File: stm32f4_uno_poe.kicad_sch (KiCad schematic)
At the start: 12 parts, among them J101 STM32 GPIO, J102 Digital/PWM, J103 STM32 GPIO, J104 STM32 GPIO, J105 STM32 GPIO, J106 Power, J107 Conn_01x04, J108 Ethernet, J109 STM32 GPIO, J110 Digital/PWM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

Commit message: WIP
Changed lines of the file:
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@@
     )
     (property "Description" "" (at 262.255 37.465 0)
-      (effects (font (size 1.27 1.27)) hide)
+      (effects (font (size 1 1)) hide)
     )
     (property "Manufacturer" "" (at 262.255 37.465 0)
-      (effects (font (size 1.27 1.27)) hide)
+      (effects (font (size 1 1)) hide)
     )
     (property "Partnumber" "" (at 262.255 37.465 0)
-      (effects (font (size 1.27 1.27)) hide)
+      (effects (font (size 1 1)) hide)
     )
     (property "JLCPCB Part #" "" (at 262.255 37.465 0)
-      (effects (font (size 1.27 1.27)) hide)
+      (effects (font (size 1 1)) hide)
     )
     (property "isBasicPart" "" (at 262.255 37.465 0)
-      (effects (font (size 1.27 1.27)) hide)
+      (effects (font (size 1 1)) hide)
     )
     (property "Description" "" (at 262.255 37.465 0)
-      (effects (font (size 1.27 1.27)) hide)
+      (effects (font (size 1 1)) hide)
     )
     (property "Manufacturer" "" (at 262.255 37.465 0)
-      (effects (font (size 1.27 1.27)) hide)
+      (effects (font (size 1 1)) hide)
     )
     (property "Partnumber" "" (at 262.255 37.465 0)
-      (effects (font (size 1.27 1.27)) hide)
+      (effects (font (size 1 1)) hide)
     )
     (property "JLCPCB Part #" "" (at 262.255 37.465 0)
-      (effects (font (size 1.27 1.27)) hide)
+      (effects (font (size 1 1)) hide)
     )
     (property "isBasicPart" "" (at 262.255 37.465 0)
-      (effects (font (size 1.27 1.27)) hide)
+      (effects (font (size 1 1)) hide)
     )
     (pin "1")
@@
     )
     (property "Description" "" (at 262.255 67.945 0)
-      (effects (font (size 1.27 1.27)) hide)
+      (effects (font (size 1 1)) hide)
     )
     (property "Manufacturer" "" (at 262.255 67.945 0)
-      (effects (font (size 1.27 1.27)) hide)
+      (effects (font (size 1 1)) hide)
     )
     (property "Partnumber" "" (at 262.255 67.945 0)
-      (effects (font (size 1.27 1.27)) hide)
+      (effects (font (size 1 1)) hide)
     )
     (property "JLCPCB Part #" "" (at 262.255 67.945 0)
-      (effects (font (size 1.27 1.27)) hide)
+      (effects (font (size 1 1)) hide)
     )
     (property "isBasicPart" "" (at 262.255 67.945 0)
-      (effects (font (size 1.27 1.27)) hide)
+      (effects (font (size 1 1)) hide)
     )
     (property "Description" "" (at 262.255 67.945 0)
-      (effects (font (size 1.27 1.27)) hide)
+      (effects (font (size 1 1)) hide)
     )
     (property "Manufacturer" "" (at 262.255 67.945 0)
-      (effects (font (size 1.27 1.27)) hide)
+      (effects (font (size 1 1)) hide)
     )
     (property "Partnumber" "" (at 262.255 67.945 0)
-      (effects (font (size 1.27 1.27)) hide)
+      (effects (font (size 1 1)) hide)
     )
     (property "JLCPCB Part #" "" (at 262.255 67.945 0)
-      (effects (font (size 1.27 1.27)) hide)
+      (effects (font (size 1 1)) hide)
     )
     (property "isBasicPart" "" (at 262.255 67.945 0)
-      (effects (font (size 1.27 1.27)) hide)
+      (effects (font (size 1 1)) hide)
     )
     (pin "1")
@@
     (in_bom yes) (on_board yes) (dnp yes) (fields_autoplaced)
     (property "Reference" "J112" (at 52.07 69.215 0)
-      (effects (font (size 1.27 1.27)))
+      (effects (font (size 1 1)))
     )
     (property "Value" "Barrel_Jack" (at 52.07 71.755 0)
-      (effects (font (size 1.27 1.27)))
+      (effects (font (size 1 1)))
     )
     (property "Footprint" "Connector_BarrelJack:BarrelJack_CUI_PJ-102AH_Horizontal" (at 53.34 78.486 0)
-      (effects (font (size 1.27 1.27)) hide)
+      (effects (font (size 1 1)) hide)
     )
     (property "Datasheet" "~" (at 53.34 78.486 0)
-      (effects (font (size 1.27 1.27)) hide)
+      (effects (font (size 1 1)) hide)
     )
     (property "Description" "" (at 52.07 77.47 0)
-      (effects (font (size 1.27 1.27)) hide)
+      (effects (font (size 1 1)) hide)
     )
     (property "Manufacturer" "CUI Devices" (at 52.07 77.47 0)
-      (effects (font (size 1.27 1.27)) hide)
+      (effects (font (size 1 1)) hide)
     )
     (property "Partnumber" "PJ-102AH" (at 52.07 77.47 0)
-      (effects (font (size 1.27 1.27)) hide)
+      (effects (font (size 1 1)) hide)
     )
     (property "JLCPCB Part #" "" (at 52.07 77.47 0)
-      (effects (font (size 1.27 1.27)) hide)
+      (effects (font (size 1 1)) hide)
     )
     (property "isBasicPart" "NO" (at 52.07 77.47 0)
-      (effects (font (size 1.27 1.27)) hide)
+      (effects (font (size 1 1)) hide)
     )
     (pin "1")
@@
     )
     (property "Description" "" (at 54.61 59.69 0)
-      (effects (font (size 1.27 1.27)) hide)
+      (effects (font (size 1 1)) hide)
     )
     (property "Manufacturer" "" (at 54.61 59.69 0)
-      (effects (font (size 1.27 1.27)) hide)
+      (effects (font (size 1 1)) hide)
     )
     (property "Partnumber" "" (at 54.61 59.69 0)
-      (effects (font (size 1.27 1.27)) hide)
+      (effects (font (size 1 1)) hide)
     )
     (property "JLCPCB Part #" "" (at 54.61 59.69 0)
-      (effects (font (size 1.27 1.27)) hide)
+      (effects (font (size 1 1)) hide)
     )
     (property "isBasicPart" "" (at 54.61 59.69 0)
-      (effects (font (size 1.27 1.27)) hide)
+      (effects (font (size 1 1)) hide)
     )
     (property "Description" "" (at 54.61 59.69 0)
-      (effects (font (size 1.27 1.27)) hide)
+      (effects (font (size 1 1)) hide)
     )
     (property "Manufacturer" "" (at 54.61 59.69 0)
-      (effects (font (size 1.27 1.27)) hide)
+      (effects (font (size 1 1)) hide)
     )
     (property "Partnumber" "" (at 54.61 59.69 0)
-      (effects (font (size 1.27 1.27)) hide)
+      (effects (font (size 1 1)) hide)
     )
     (property "JLCPCB Part #" "" (at 54.61 59.69 0)
-      (effects (font (size 1.27 1.27)) hide)
+      (effects (font (size 1 1)) hide)
     )
     (property "isBasicPart" "" (at 54.61 59.69 0)
-      (effects (font (size 1.27 1.27)) hide)
+      (effects (font (size 1 1)) hide)
     )
     (pin "1")
@@
     )
     (property "Description" "" (at 204.47 42.545 0)
-      (effects (font (size 1.27 1.27)) hide)
+      (effects (font (size 1 1)) hide)
     )
     (property "Manufacturer" "" (at 204.47 42.545 0)
-      (effects (font (size 1.27 1.27)) hide)
+      (effects (font (size 1 1)) hide)
     )
     (property "Partnumber" "" (at 204.47 42.545 0)
-      (effects (font (size 1.27 1.27)) hide)
+      (effects (font (size 1 1)) hide)
     )
     (property "JLCPCB Part #" "" (at 204.47 42.545 0)
-      (effects (font (size 1.27 1.27)) hide)
+      (effects (font (size 1 1)) hide)
     )
     (property "isBasicPart" "" (at 204.47 42.545 0)
-      (effects (font (size 1.27 1.27)) hide)
+      (effects (font (size 1 1)) hide)
     )
     (property "Description" "" (at 204.47 42.545 0)
-      (effects (font (size 1.27 1.27)) hide)
+      (effects (font (size 1 1)) hide)
     )
     (property "Manufacturer" "" (at 204.47 42.545 0)
-      (effects (font (size 1.27 1.27)) hide)
+      (effects (font (size 1 1)) hide)
     )
     (property "Partnumber" "" (at 204.47 42.545 0)
-      (effects (font (size 1.27 1.27)) hide)
+      (effects (font (size 1 1)) hide)
     )
     (property "JLCPCB Part #" "" (at 204.47 42.545 0)
-      (effects (font (size 1.27 1.27)) hide)
+      (effects (font (size 1 1)) hide)
     )
     (property "isBasicPart" "" (at 204.47 42.545 0)
-      (effects (font (size 1.27 1.27)) hide)
+      (effects (font (size 1 1)) hide)
     )
     (pin "1")
@@
     )
     (property "Description" "" (at 204.47 67.945 0)
-      (effects (font (size 1.27 1.27)) hide)
+      (effects (font (size 1 1)) hide)
     )
     (property "Manufacturer" "" (at 204.47 67.945 0)
-      (effects (font (size 1.27 1.27)) hide)
+      (effects (font (size 1 1)) hide)
     )
     (property "Partnumber" "" (at 204.47 67.945 0)
-      (effects (font (size 1.27 1.27)) hide)
+      (effects (font (size 1 1)) hide)
     )
     (property "JLCPCB Part #" "" (at 204.47 67.945 0)
-      (effects (font (size 1.27 1.27)) hide)
+      (effects (font (size 1 1)) hide)
     )
     (property "isBasicPart" "" (at 204.47 67.945 0)
-      (effects (font (size 1.27 1.27)) hide)
+      (effects (font (size 1 1)) hide)
     )
     (property "Description" "" (at 204.47 67.945 0)
-      (effects (font (size 1.27 1.27)) hide)
+      (effects (font (size 1 1)) hide)
     )
     (property "Manufacturer" "" (at 204.47 67.945 0)
-      (effects (font (size 1.27 1.27)) hide)
+      (effects (font (size 1 1)) hide)
     )
     (property "Partnumber" "" (at 204.47 67.945 0)
-      (effects (font (size 1.27 1.27)) hide)
+      (effects (font (size 1 1)) hide)
     )
     (property "JLCPCB Part #" "" (at 204.47 67.945 0)
-      (effects (font (size 1.27 1.27)) hide)
+      (effects (font (size 1 1)) hide)
     )
     (property "isBasicPart" "" (at 204.47 67.945 0)
-      (effects (font (size 1.27 1.27)) hide)
-    )
-    (pin "1")
+      (effects (font (size 1 1)) hide)
+    )
+    (pin "1")

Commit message: WIP
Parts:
- added J113: Conn_01x02, symbol Connector_Generic:Conn_01x02
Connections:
- net GND: now also J113.2 (Pin_2)
- net PoE/24V: now also J113.1 (Pin_1)
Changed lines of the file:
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@@
     (stroke (width 0) (type solid))
+  )
+  (wire (pts (xy 119.38 57.15) (xy 123.19 57.15))
+    (stroke (width 0) (type default))
   )
   (wire (pts (xy 172.085 78.105) (xy 184.785 78.105))
@@
   )
   (wire (pts (xy 176.53 45.085) (xy 184.785 45.085))
+    (stroke (width 0) (type default))
+  )
+  (wire (pts (xy 123.19 62.23) (xy 123.19 59.69))
     (stroke (width 0) (type default))
   )
@@
     )
   )
+  (symbol (lib_id "Connector_Generic:Conn_01x02") (at 128.27 57.15 0) (unit 1)
+    (in_bom yes) (on_board yes) (dnp no) (fields_autoplaced)
+    (property "Reference" "J113" (at 130.81 57.15 0)
+      (effects (font (size 1.27 1.27)) (justify left))
+    )
+    (property "Value" "Conn_01x02" (at 130.81 59.69 0)
+      (effects (font (size 1.27 1.27)) (justify left))
+    )
+    (property "Footprint" "" (at 128.27 57.15 0)
+      (effects (font (size 1.27 1.27)) hide)
+    )
+    (property "Datasheet" "~" (at 128.27 57.15 0)
+      (effects (font (size 1.27 1.27)) hide)
+    )
+    (pin "1")
+    (pin "2")
+    (instances
+      (project "stm32f4_uno_poe"
+        (path "/e63e39d7-6ac0-4ffd-8aa3-1841a4541b55"
+          (reference "J113") (unit 1)
+        )
+      )
+    )
+  )
   (symbol (lib_id "power:GND") (at 258.445 55.245 90) (unit 1)
     (in_bom yes) (on_board yes) (dnp no)
@@
         )
       )
+    )
+  )
+  (symbol (lib_id "power:GND") (at 123.19 62.23 0) (unit 1)
+    (in_bom yes) (on_board yes) (dnp no)
+    (property "Reference" "#PWR0108" (at 123.19 68.58 0)
+      (effects (font (size 1 1)) hide)
+    )
+    (property "Value" "GND" (at 123.19 66.675 90)
+      (effects (font (size 1 1)))
+    )
+    (property "Footprint" "" (at 123.19 62.23 0)
+      (effects (font (size 1 1)))
+    )
+    (property "Datasheet" "" (at 123.19 62.23 0)
+      (effects (font (size 1 1)))
+    )
+    (pin "1")
+    (instances
+      (project "stm32f4_uno_poe"
+        (path "/e63e39d7-6ac0-4ffd-8aa3-1841a4541b55"
+          (reference "#PWR0108") (unit 1)
+        )
+      )

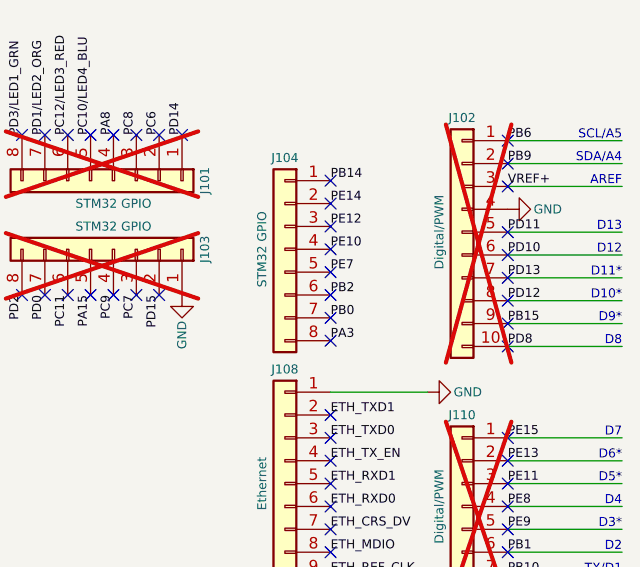
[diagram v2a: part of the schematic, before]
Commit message: Add ETH_RXER
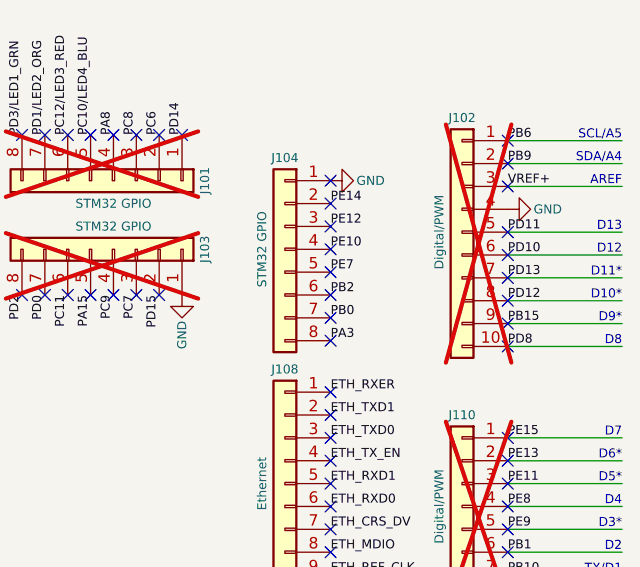
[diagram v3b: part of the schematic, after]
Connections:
- net PB14 is gone; now on net GND: J104.1 (Pin_1)
- net GND: no longer J108.1 (Pin_1)
- new net ETH_RXER: J108.1 (Pin_1)
- no-connect marks 74 -> 75
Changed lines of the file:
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@@
   (junction (at 176.53 47.625) (diameter 0) (color 0 0 0 0)
   )
+  (no_connect (at 247.65 55.245))
   (no_connect (at 267.335 75.565))
   (no_connect (at 199.39 47.625))
@@
     (stroke (width 0) (type default))
   )
-  (wire (pts (xy 247.65 55.245) (xy 258.445 55.245))
-    (stroke (width 0) (type default))
-  )
   (wire (pts (xy 267.335 50.165) (xy 280.035 50.165))
     (stroke (width 0) (type solid))
@@
     (effects (font (size 1 1)) (justify right bottom))
   )
-  (label "PB14" (at 247.65 31.75 0) (fields_autoplaced)
-    (effects (font (size 1 1)) (justify left bottom))
-  )
   (label "ETH_RXD0" (at 247.65 67.945 0) (fields_autoplaced)
     (effects (font (size 1 1)) (justify left bottom))
@@
   )
   (label "PC6" (at 228.6 26.67 90) (fields_autoplaced)
+    (effects (font (size 1 1)) (justify left bottom))
+  )
+  (label "ETH_RXER" (at 247.65 55.245 0) (fields_autoplaced)
     (effects (font (size 1 1)) (justify left bottom))
   )
@@
     )
   )
-  (symbol (lib_id "power:GND") (at 258.445 55.245 90) (unit 1)
-    (in_bom yes) (on_board yes) (dnp no)
-    (property "Reference" "#PWR0106" (at 264.795 55.245 0)
-      (effects (font (size 1 1)) hide)
-    )
-    (property "Value" "GND" (at 262.89 55.245 90)
-      (effects (font (size 1 1)))
-    )
-    (property "Footprint" "" (at 258.445 55.245 0)
-      (effects (font (size 1 1)))
-    )
-    (property "Datasheet" "" (at 258.445 55.245 0)
-      (effects (font (size 1 1)))
-    )
-    (pin "1")
-    (instances
-      (project "stm32f4_uno_poe"
-        (path "/e63e39d7-6ac0-4ffd-8aa3-1841a4541b55"
-          (reference "#PWR0106") (unit 1)
-        )
-      )
-    )
-  )
   (symbol (lib_id "power:+5V") (at 176.53 47.625 90) (unit 1)
     (in_bom yes) (on_board yes) (dnp no)
@@
         )
       )
+    )
+  )
+  (symbol (lib_id "power:GND") (at 247.65 31.75 90) (unit 1)
+    (in_bom yes) (on_board yes) (dnp no)
+    (property "Reference" "#PWR0106" (at 254 31.75 0)
+      (effects (font (size 1 1)) hide)
+    )
+    (property "Value" "GND" (at 252.095 31.75 90)
+      (effects (font (size 1 1)))
+    )
+    (property "Footprint" "" (at 247.65 31.75 0)
+      (effects (font (size 1 1)))
+    )
+    (property "Datasheet" "" (at 247.65 31.75 0)
+      (effects (font (size 1 1)))
+    )
+    (pin "1")
+    (instances
+      (project "stm32f4_uno_poe"
+        (path "/e63e39d7-6ac0-4ffd-8aa3-1841a4541b55"
+          (reference "#PWR0106") (unit 1)
+        )
+      )
